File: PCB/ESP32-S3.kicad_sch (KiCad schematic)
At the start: 7 parts, among them J1 USB_C_Receptacle_USB2.0_16P

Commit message: Uhh tesst
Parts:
- removed D2, D3, D4: LESD5D5.0CT1G, LESD5D5.0CT1G:TVS_LESD5D5.0CT1G, symbol LESD5D5.0CT1G:LESD5D5.0CT1G
- added D2: LESD5D5.0CT1G, LESD5D5.0CT1G:TVS_LESD5D5.0CT1G, symbol WALL-E_SYM:LESD5D5.0CT1G

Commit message: [Schem] Uhh made the Amplifier & motor driver circuits
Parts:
- removed D1: 1N5819WS, Diode_SMD:D_SOD-323, symbol Diode:1N5819WS
- removed D2: LESD5D5.0CT1G, LESD5D5.0CT1G:TVS_LESD5D5.0CT1G, symbol WALL-E_SYM:LESD5D5.0CT1G
- removed J1: USB_C_Receptacle_USB2.0_16P, symbol Connector:USB_C_Receptacle_USB2.0_16P
- removed R1, R2: R, symbol Device:R
- added C10, C12, C4, C6, C7, C8: 0.1 uF, Capacitor_SMD:C_0603_1608Metric_Pad1.08x0.95mm_HandSolder, symbol Device:C
- added C11: 1uF, Capacitor_SMD:C_0603_1608Metric_Pad1.08x0.95mm_HandSolder, symbol Device:C
- added C2: 10uf, Capacitor_SMD:C_0603_1608Metric_Pad1.08x0.95mm_HandSolder, symbol Device:C
- added C3, C5, C9: 10uF, Capacitor_SMD:C_0603_1608Metric_Pad1.08x0.95mm_HandSolder, symbol Device:C
- added D1: SK6812, LED_SMD:LED_SK6812_PLCC4_5.0x5.0mm_P3.2mm, symbol LED:SK6812
- added D2, D3, D4: LESD5D5.0CT1G, LESD5D5.0CT1G:TVS_LESD5D5.0CT1G, symbol WALL-E_symbols:LESD5D5.0CT1G
- added D5: 1N5819WS, Diode_SMD:D_SOD-323, symbol Diode:1N5819WS
- added D6: LED, LED_SMD:LED_0603_1608Metric_Pad1.05x0.95mm_HandSolder, symbol Device:LED
- added J2: USB_C_Receptacle_USB2.0_16P, Connector_USB:USB_C_Receptacle_Amphenol_12401610E4-2A_CircularHoles, symbol Connector:USB_C_Receptacle_USB2.0_16P
- added R3, R4: 5k, Resistor_SMD:R_0603_1608Metric_Pad0.98x0.95mm_HandSolder, symbol Device:R
- added R5, R6, R7, R8: 10k, Resistor_SMD:R_0603_1608Metric_Pad0.98x0.95mm_HandSolder, symbol Device:R
- added R9: 7.5k, Resistor_SMD:R_0603_1608Metric_Pad0.98x0.95mm_HandSolder, symbol Device:R
- added SW1, SW2, SW3: SW_MEC_5E, RAM:SW_Push_1P1T_NO_CK_KMR2, symbol Switch:SW_MEC_5E
- added U1: ESP32-S3-WROOM-1, RF_Module:ESP32-S3-WROOM-1, symbol RF_Module:ESP32-S3-WROOM-1
- added U3: AMS1117-3.3, Package_TO_SOT_SMD:SOT-223-3_TabPin2, symbol Regulator_Linear:AMS1117-3.3
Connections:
- new net: D6.2 (A), R9.2
- new net: D4.2, D5.2 (A), J2.A4 (VBUS), J2.A9 (VBUS), J2.B4 (VBUS), J2.B9 (VBUS)
- new net: J2.A5 (CC1), R3.1
- new net: J2.B5 (CC2), R4.1
- new net 0RX: U1.36 (RXD0)
- new net 0TX: U1.37 (TXD0)
- new net Add_but: C8.1, R8.1, SW3.3 (K), SW3.4 (A)
- new net CHIP_PU: C11.1, C7.1, R6.1, R7.1, SW2.3 (K), SW2.4 (A), U1.3 (EN)
- new net Dn: D2.2, J2.A6 (D+), J2.B6 (D+), U1.13 (USB_D-)
- new net Dp: D3.2, J2.A7 (D-), J2.B7 (D-), U1.14 (USB_D+)
- new net ESP_3v3: C10.1, C12.1, C5.1, C9.1, D1.3 (VDD), R5.2, R6.2, R7.2, R8.2, R9.1, U1.2 (3V3), U3.2 (VO)
- new net GND: C10.2, C11.2, C12.2, C2.2, C3.2, C4.2, C5.2, C6.2, C7.2, C8.2, C9.2, D1.1 (VSS), D2.1, D3.1, D4.1, D6.1 (K), J2.A1 (GND), J2.A12 (GND), J2.B1 (GND), J2.B12 (GND), J2.SH (SHIELD), R3.2, R4.2, SW2.1, SW2.2, SW3.1, SW3.2, U1.1 (GND), U1.40 (GND), U1.41 (GND), U3.1 (GND)
- new net GPIO1: U1.39 (IO1)
- new net GPIO10: U1.18 (IO10)
- new net GPIO11: U1.19 (IO11)
- new net GPIO12: U1.20 (IO12)
- new net GPIO13: U1.21 (IO13)
- new net GPIO14: U1.22 (IO14)
- new net GPIO15: U1.8 (IO15)
- new net GPIO17: U1.10 (IO17), U1.9 (IO16)
- new net GPIO18: U1.11 (IO18)
- new net GPIO2: U1.38 (IO2)
- new net GPIO21: U1.23 (IO21)
- new net GPIO3: U1.15 (IO3)
- new net GPIO39: U1.32 (IO39)
- new net GPIO4: U1.4 (IO4)
- new net GPIO40: U1.33 (IO40)
- new net GPIO41: U1.34 (IO41)
- new net GPIO42: U1.35 (IO42)
- new net GPIO45: U1.26 (IO45)
- new net GPIO46: U1.16 (IO46)
- new net GPIO48: U1.25 (IO48)
- new net GPIO5: U1.5 (IO5)
- new net GPIO6: U1.6 (IO6)
- new net GPIO7: U1.7 (IO7)
- new net GPIO8: U1.12 (IO8)
- new net GPIO9: U1.17 (IO9)
- new net GPIO_0: C6.1, R5.1, SW1.3 (K), SW1.4 (A), U1.27 (IO0)
- new net IO38: U1.31 (IO38)
- new net RGB: D1.2 (DIN), U1.24 (IO47)
- new net RGBout: D1.4 (DOUT)
- new net VCC_5v: C2.1, C3.1, C4.1, D5.1 (K), U3.3 (VI)
- no-connect marks 0 -> 5

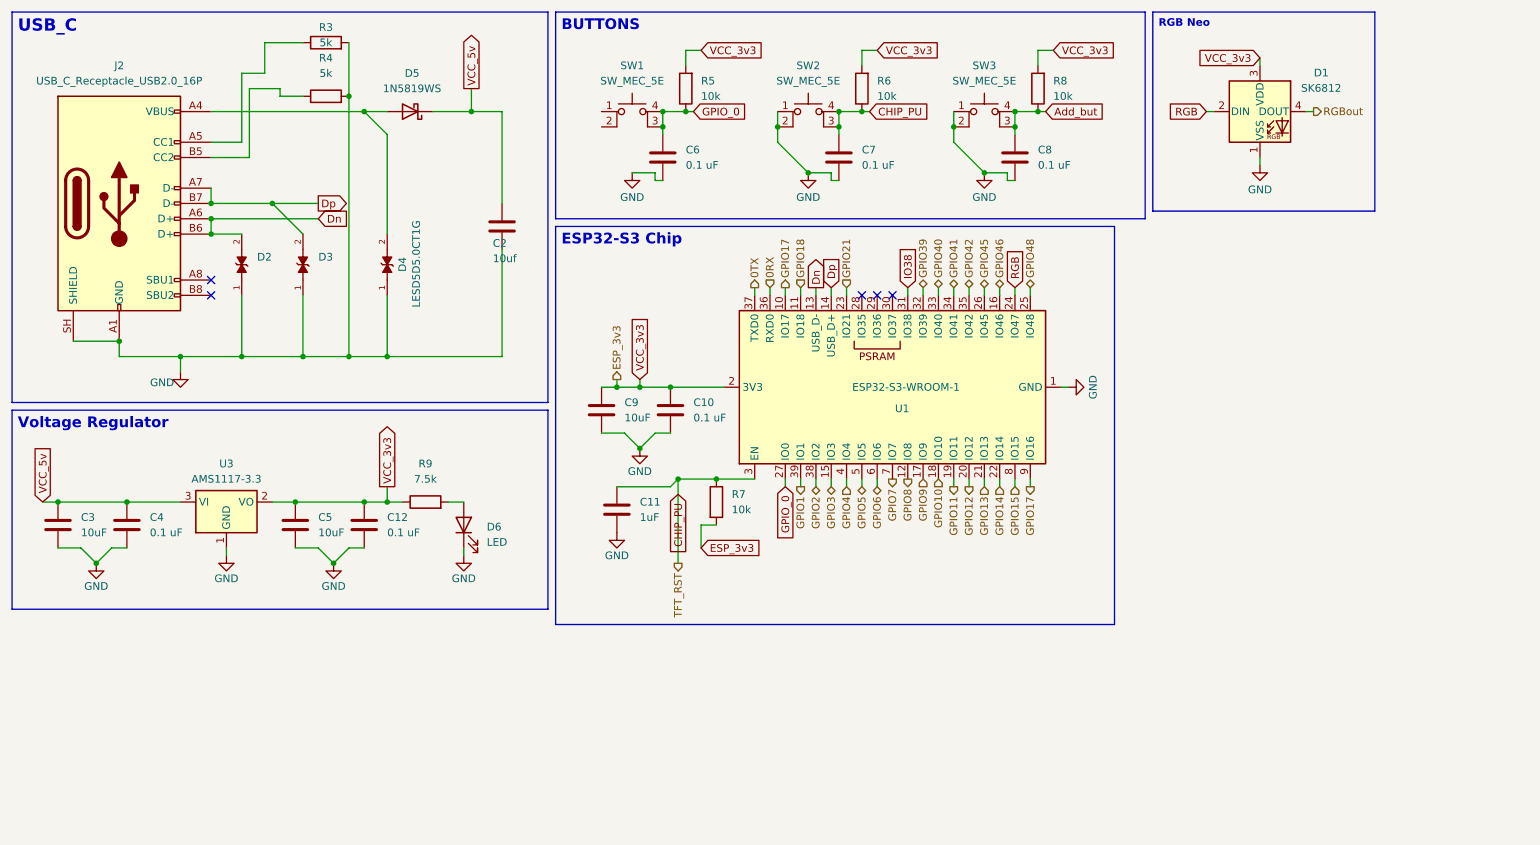
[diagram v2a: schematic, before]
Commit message: [Schem] Added sensors connectors & finished Step down circuit
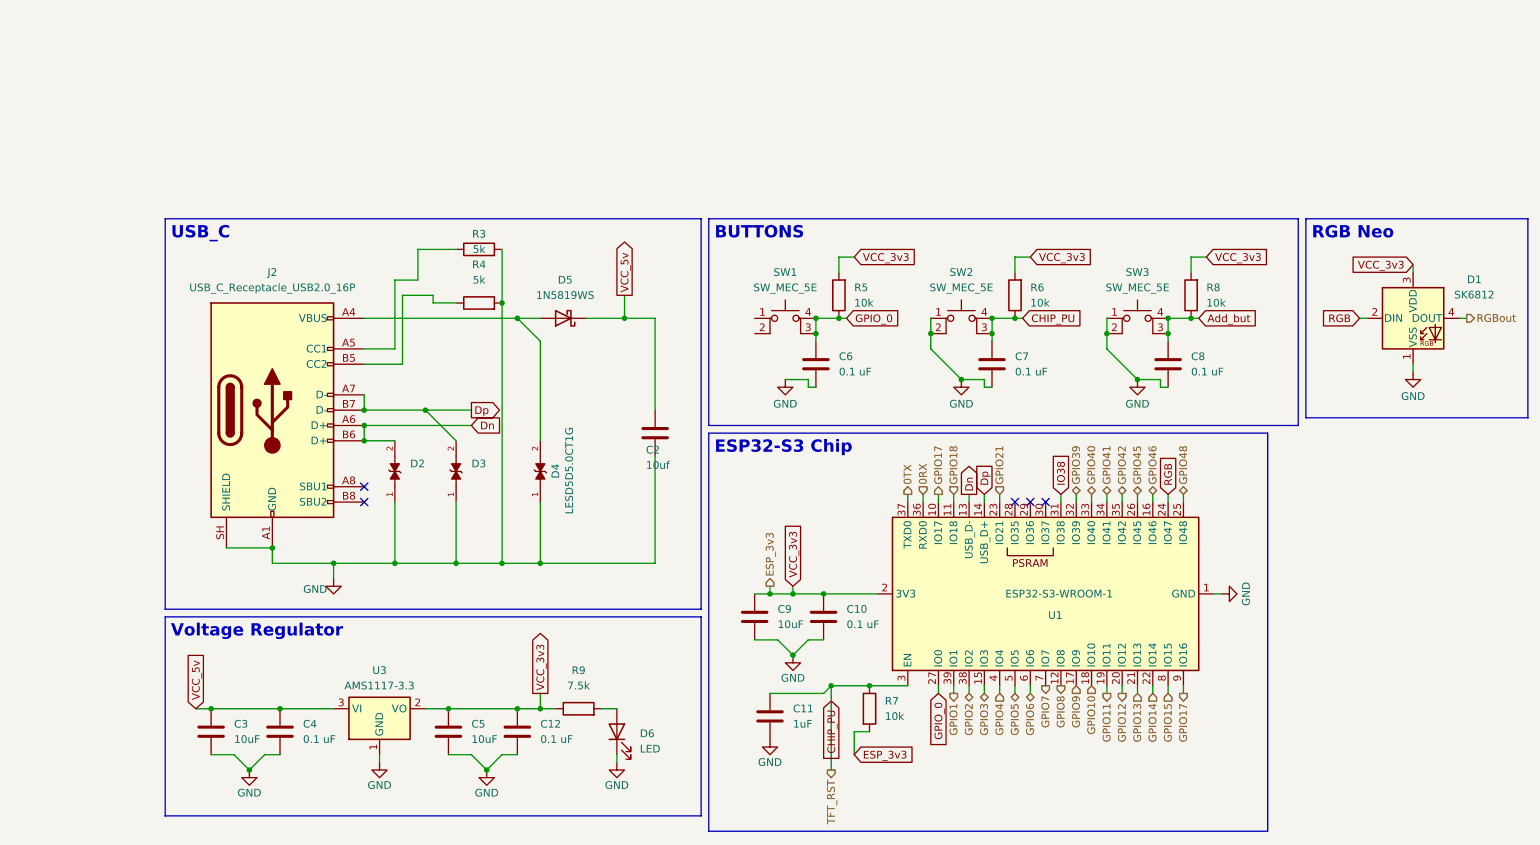
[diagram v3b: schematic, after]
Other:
- moved on the sheet: C10, C11, C12, C2, C3, C4, C5, C6, C7, C8, C9, D1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

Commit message: [Schem] Finished the Hierarchy Labels of all the pages
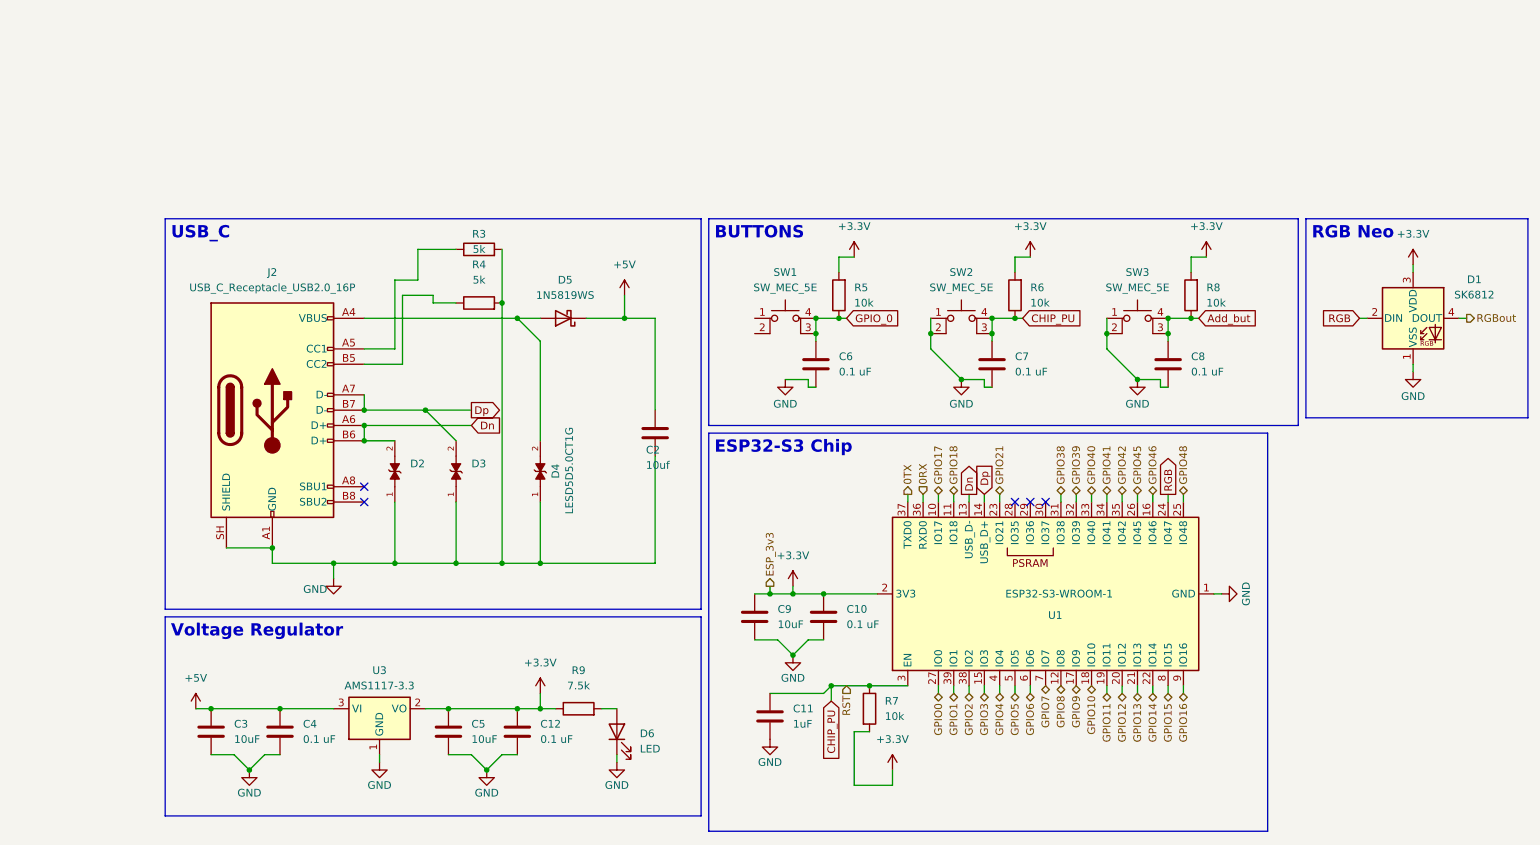
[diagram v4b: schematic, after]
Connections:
- net GPIO17: no longer U1.9 (IO16)
- net GPIO_0: no longer U1.27 (IO0)
- net ESP_3v3 renamed +3.3V
- net IO38 renamed GPIO38
- net VCC_5v renamed +5V
- new net GPIO0: U1.27 (IO0)
- new net GPIO16: U1.9 (IO16)

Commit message: [PCB] Assigned all the footprints
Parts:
- added J13: Debug, Connector_JST:JST_ZH_B4B-ZR-SM4-TF_1x04-1MP_P1.50mm_Vertical, symbol Connector_Generic:Conn_01x04
- D2, D3, D4: footprint LESD5D5.0CT1G:TVS_LESD5D5.0CT1G -> Battery-extra:TVS_LESD5D5.0CT1G
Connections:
- net +3.3V: now also J13.4 (Pin_4)
- net 0RX: now also J13.2 (Pin_2)
- net 0TX: now also J13.1 (Pin_1)
- net GND: now also J13.3 (Pin_3)

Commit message: [PCB] Traced the ESP's Type C
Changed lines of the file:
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@@
 		(in_pos_files yes)
 		(dnp no)
-		(fields_autoplaced yes)
 		(property "Reference" "R4"
-			(at 91.44 55.88 90)
+			(at 91.44 59.944 90)
 			(show_name no)
 			(do_not_autoplace no)
@@
 		)
 		(property "Value" "5k"
-			(at 91.44 58.42 90)
+			(at 91.44 62.23 90)
 			(show_name no)
 			(do_not_autoplace no)

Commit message: [PCB] Connected BTs & USB to the ESP
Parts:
- removed C8: 0.1 uF, Capacitor_SMD:C_0603_1608Metric_Pad1.08x0.95mm_HandSolder, symbol Device:C
- removed R8: 10k, Resistor_SMD:R_0603_1608Metric_Pad0.98x0.95mm_HandSolder, symbol Device:R
- removed SW3: SW_MEC_5E, RAM:SW_Push_1P1T_NO_CK_KMR2, symbol Switch:SW_MEC_5E
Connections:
- net GPIO0 is gone; now on net GPIO_0: U1.27 (IO0)
- net GND: now also SW1.1, SW1.2
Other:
- moved on the sheet: D1

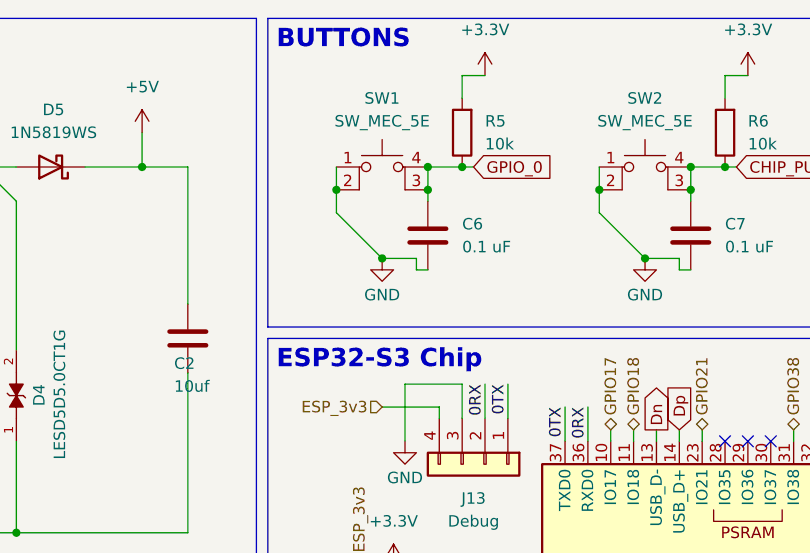
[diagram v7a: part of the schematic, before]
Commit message: [PCB] 95% finished the PCB
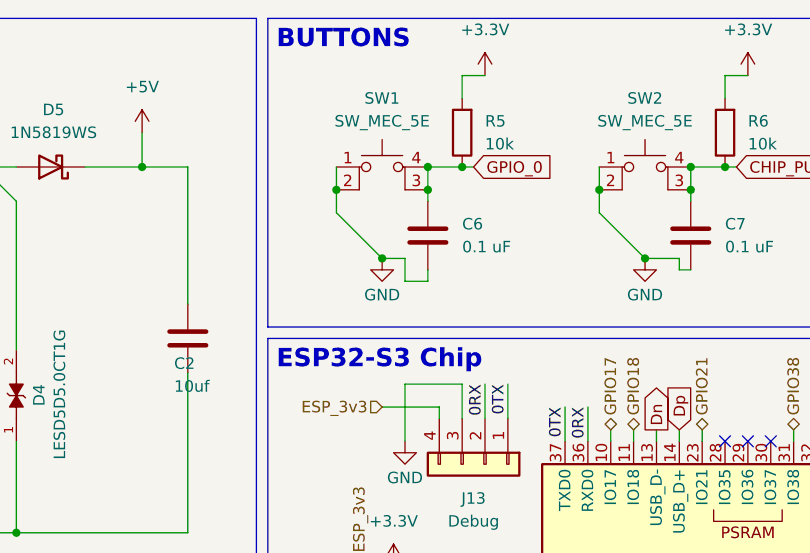
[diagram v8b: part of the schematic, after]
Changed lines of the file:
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@@
+	(wire
+		(pts
+			(xy 144.78 77.47) (xy 147.32 77.47)
+		)
+		(stroke
+			(width 0)
+			(type default)
+		)
+	)
 	(wire
 		(pts
@@
 	(wire
 		(pts
-			(xy 146.05 76.2) (xy 147.32 76.2)
-		)
-		(stroke
-			(width 0)
-			(type default)
-		)
-	)
-	(wire
-		(pts
 			(xy 101.6 129.54) (xy 104.14 129.54)
 		)
@@
 	(wire
 		(pts
+			(xy 147.32 76.2) (xy 147.32 77.47)
+		)
+		(stroke
+			(width 0)
+			(type default)
+		)
+	)
+	(wire
+		(pts
 			(xy 170.18 93.98) (xy 170.18 95.25)
 		)
@@
 	(wire
 		(pts
+			(xy 144.78 74.93) (xy 142.24 74.93)
+		)
+		(stroke
+			(width 0)
+			(type default)
+		)
+	)
+	(wire
+		(pts
 			(xy 208.28 93.98) (xy 208.28 95.25)
 		)
@@
 	(wire
 		(pts
-			(xy 146.05 76.2) (xy 146.05 74.93)
-		)
-		(stroke
-			(width 0)
-			(type default)
-		)
-	)
-	(wire
-		(pts
 			(xy 193.04 93.98) (xy 193.04 95.25)
 		)
@@
 	(wire
 		(pts
+			(xy 144.78 74.93) (xy 144.78 77.47)
+		)
+		(stroke
+			(width 0)
+			(type default)
+		)
+	)
+	(wire
+		(pts
 			(xy 83.82 60.96) (xy 78.74 60.96)
 		)
@@
 		)
 		(stroke
-			(width 0)
-			(type default)
-		)
-	)
-	(wire
-		(pts
-			(xy 146.05 74.93) (xy 142.24 74.93)
-		)
-		(stroke
